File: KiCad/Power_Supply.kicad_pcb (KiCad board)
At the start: 4 copper layers, 59.7 x 64.9 mm, 54 parts, among them IC1 TPS63070RNMR, IC2 ISL23511WFB8Z, IC3 LDO40LPU33RY, J1 Jack-DC, J10 BTM_OUT, J2 USB_B, J3 LCD_connector, J4 SWD, J5 TOP_OUT, U1 STM32F401RBTx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

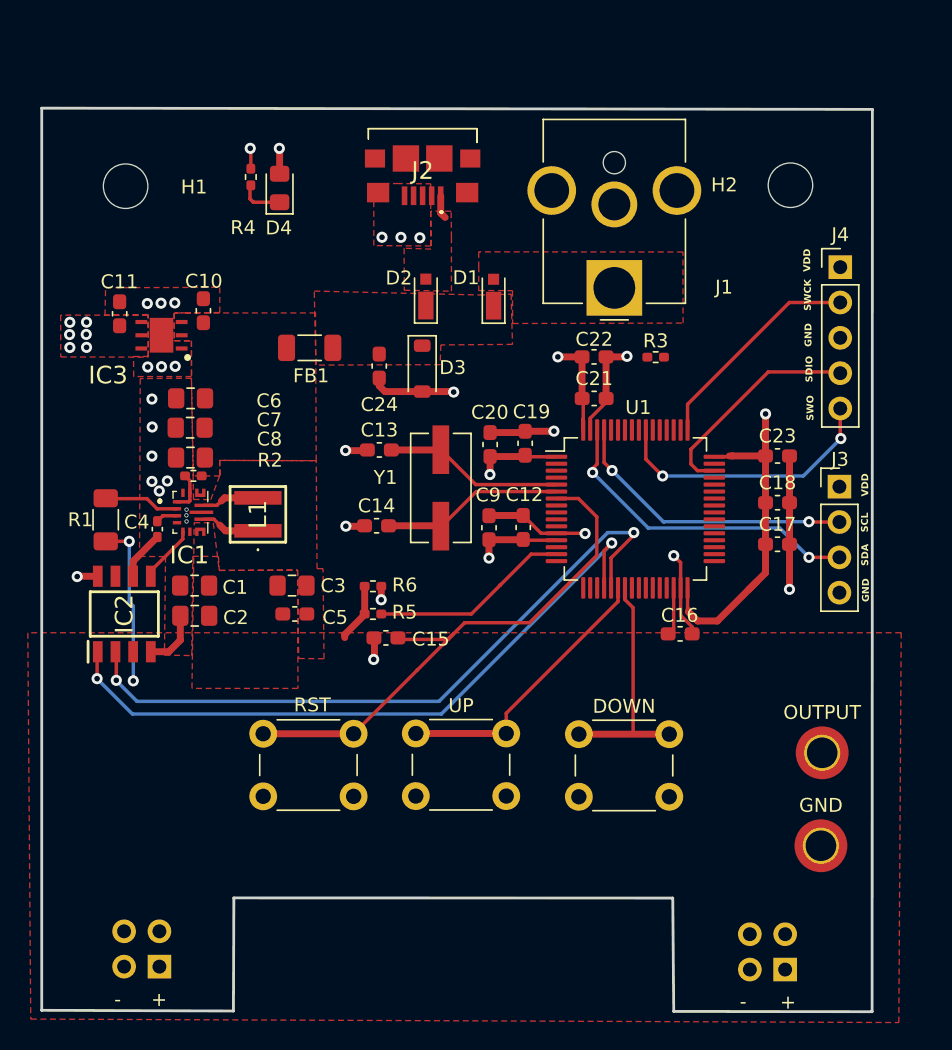
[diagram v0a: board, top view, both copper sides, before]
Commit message: Boot-0 and button layout updated.
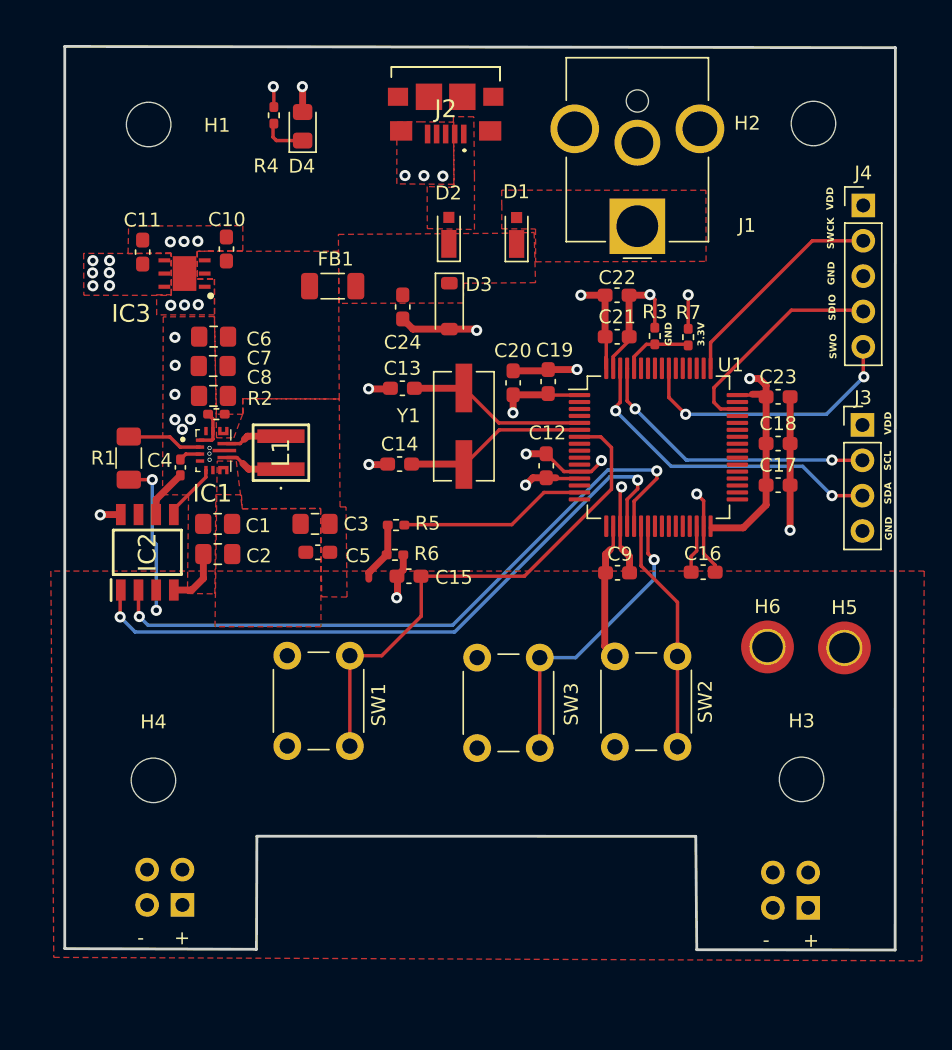
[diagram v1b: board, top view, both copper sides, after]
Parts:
- added H3: MountingHole, MountingHole:MountingHole_3.2mm_M3, F.Cu at (161.8, 100.1)
- added H4: MountingHole, MountingHole:MountingHole_3.2mm_M3, F.Cu at (115.2, 100.2)
- added R7: 1K, Resistor_SMD:R_0402_1005Metric_Pad0.72x0.64mm_HandSolder, F.Cu at (153.7, 68.3)
- D3: value 25V+ -> 30V+
- R5: value 100 -> 300
- R6: value 300 -> 1K2
- moved SW2 19.6 mm to (152.9, 91.3), turned to -90 degrees
- moved H6 14.8 mm to (159.3, 90.6)
- moved C9 9.79 mm to (148.6, 85.3), turned to 0 degrees
- moved H5 7.71 mm to (164.9, 90.7)
- moved R5 6.60 mm to (132.7, 81.8)
- moved SW3 6.18 mm to (143.0, 91.4), turned to -90 degrees
- moved SW1 5.98 mm to (124.8, 97.7), turned to 90 degrees
- moved D3 4.90 mm to (136.5, 66.1)
- moved C1 4.73 mm to (119.8, 81.8)
- moved C13 4.73 mm to (133.1, 72.0)
- moved C14 4.73 mm to (132.9, 77.5)
- moved C16 4.73 mm to (154.7, 85.2)
- moved C19 4.73 mm to (143.6, 71.5)
- moved C20 4.73 mm to (141.1, 71.6)
- moved C21 4.73 mm to (148.5, 68.3)
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- renumbered OUTPUT to H5, GND to H6, RST to SW1, UP to SW2, DOWN to SW3
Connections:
- IC1 pad 16: Main_in -> (no net)
- IC1 pad 17: ADC -> (no net)
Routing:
- net GND: track 56.0 -> 67.8 mm
- net /BOOT: track 0.00 -> 5.14 mm
- net POT_BTN_UP: track 20.3 -> 16.9 mm
- net /NRST: track 39.6 -> 37.6 mm
- net /MCU_POWER/USB_OUT: track 1.70 -> 0.00 mm
- net +3.3V: track 48.7 -> 47.3 mm, vias 12 -> 14
- net PD: track 49.6 -> 48.7 mm
- net Net-(U1-PA1): track 14.4 -> 13.6 mm
- net PU: track 48.6 -> 48.0 mm
- net ADC: track 16.1 -> 15.5 mm
- net POT_BTN_DWN: track 21.2 -> 21.0 mm, vias 0 -> 1
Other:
- board text added: "3.3V"

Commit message: Added some notes and extra ground vias.
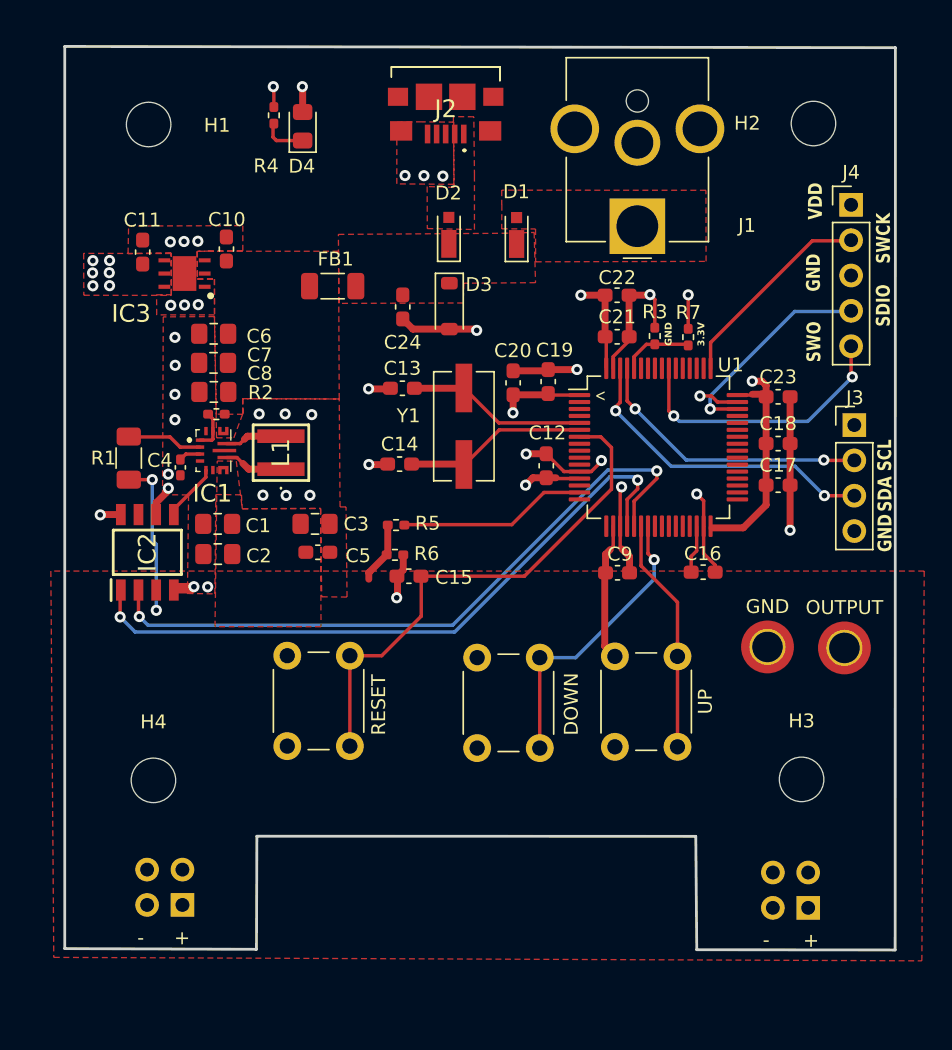
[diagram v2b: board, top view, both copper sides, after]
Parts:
- moved J4 0.88 mm to (165.4, 58.8)
- moved J3 0.59 mm to (165.6, 74.7)
- moved C8 0.29 mm to (119.5, 72.3)
- moved C7 0.23 mm to (119.5, 70.2)
- moved C6 0.21 mm to (119.5, 68.1)
- renumbered SW3 to DOWN, H6 to GND, H5 to OUTPUT, SW1 to RESET, SW2 to UP
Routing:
- net +3.3V: track 47.3 -> 46.2 mm
- net SWCLK: track 15.9 -> 15.0 mm
- net GND: track 67.8 -> 67.3 mm, vias 29 -> 35
- net SWDIO: track 16.0 -> 15.6 mm, vias 0 -> 1
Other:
- board text added: "<"

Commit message: Starting revision 1.1
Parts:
- C24: value 16pF -> 100nF
- C5: footprint Capacitor_SMD:C_0603_1608Metric_Pad1.08x0.95mm_HandSolder -> Capacitor_SMD:C_0805_2012Metric_Pad1.18x1.45mm_HandSolder
- R5: value 300 -> 2K1
- moved R6 2.20 mm to (132.6, 81.8), turned to 0 degrees
- moved R5 2.00 mm to (132.6, 83.8), turned to 0 degrees
- moved C5 0.29 mm to (126.9, 84.1)
- renumbered OUTPUT to H5, GND to H6, RESET to SW1, UP to SW2, DOWN to SW3
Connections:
- R5 pad 1: Net-(U1-PA1) -> ADC
- R5 pad 2: ADC -> Net-(U1-PA1)
- R6 pad 2: ADC -> Net-(U1-PA1)
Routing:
- net GND: track 67.3 -> 69.9 mm
- net Net-(U1-PA1): track 13.6 -> 15.6 mm
- net ADC: track 15.5 -> 14.7 mm
- net SCL: track 21.0 -> 20.4 mm

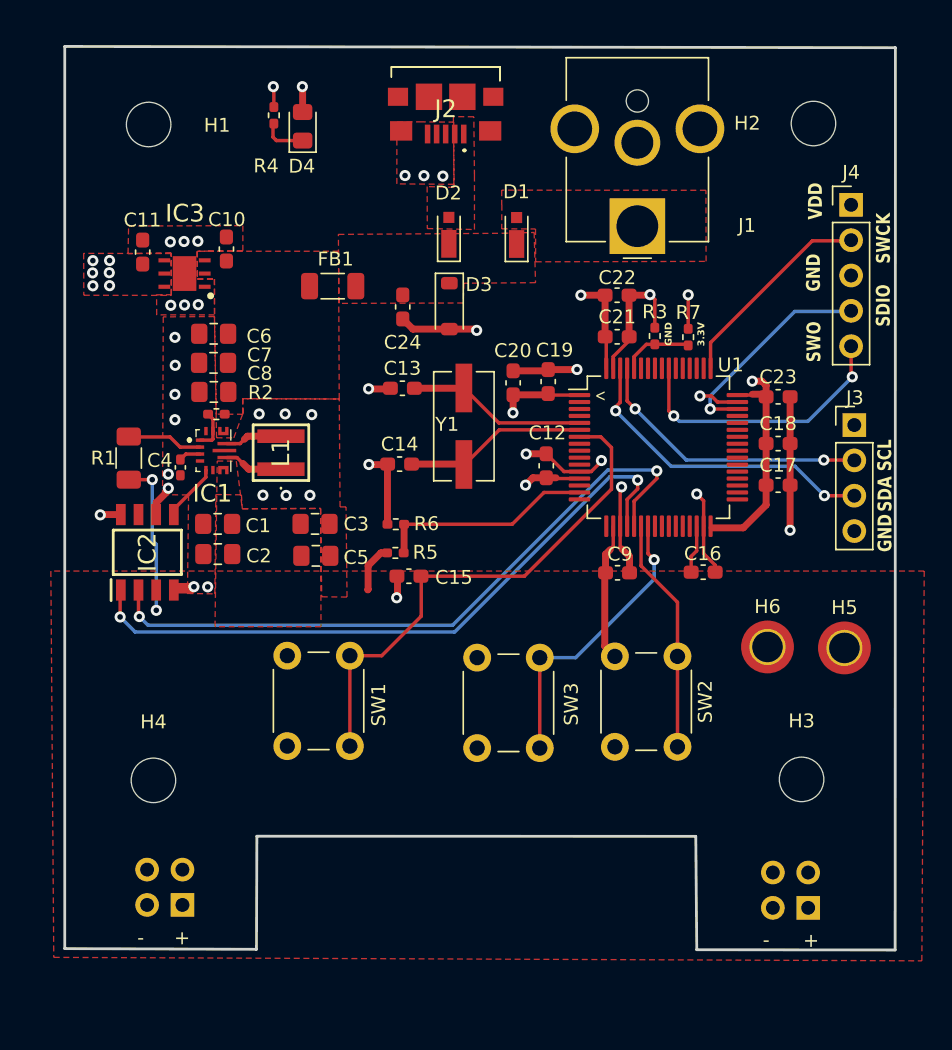
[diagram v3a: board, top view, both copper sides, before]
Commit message: pushing ofr system reset
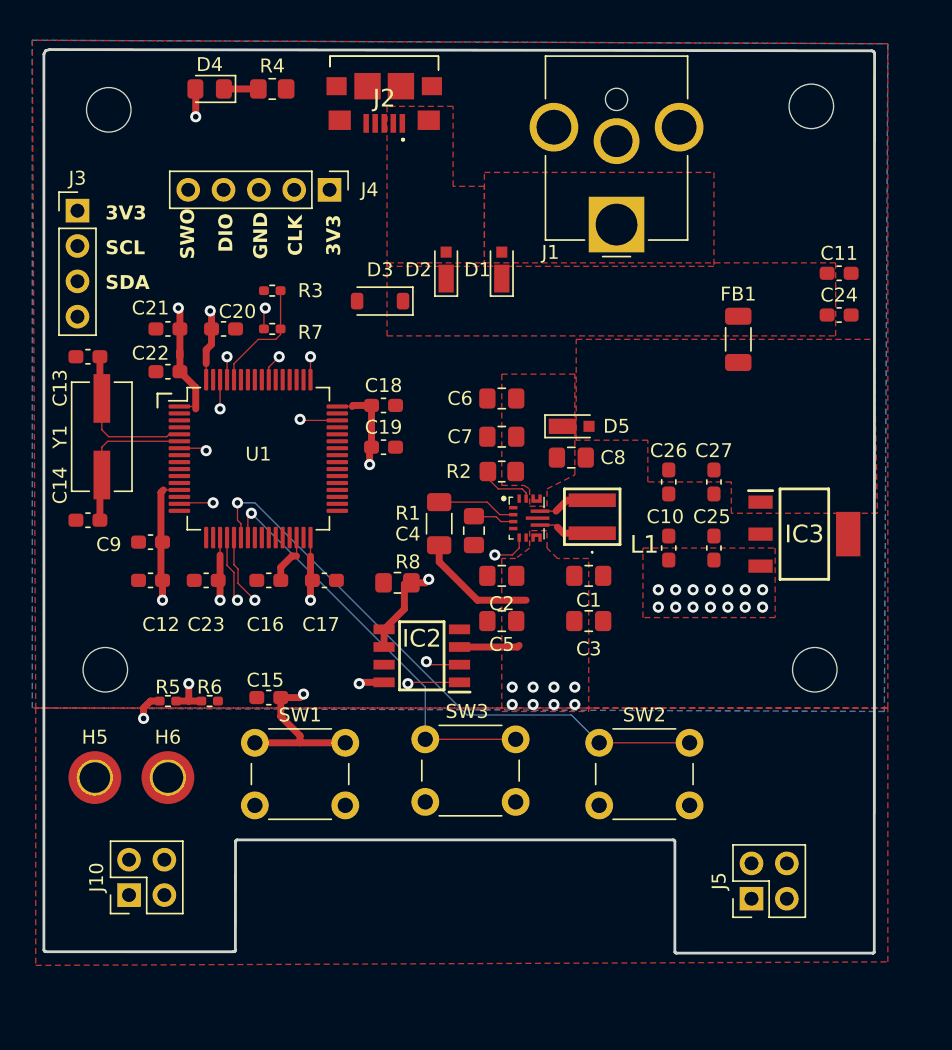
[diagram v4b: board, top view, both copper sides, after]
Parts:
- added C25: .1uF, Capacitor_SMD:C_0603_1608Metric_Pad1.08x0.95mm_HandSolder, F.Cu at (155.5, 83.5)
- added C26: 1uF, Capacitor_SMD:C_0603_1608Metric_Pad1.08x0.95mm_HandSolder, F.Cu at (152.2, 78.8)
- added C27: .1uF, Capacitor_SMD:C_0603_1608Metric_Pad1.08x0.95mm_HandSolder, F.Cu at (155.5, 78.8)
- added D5: D_Schottky, Diode_SMD:D_MicroSMP_AK, F.Cu at (145.5, 74.8)
- added R8: 953, Resistor_SMD:R_0805_2012Metric_Pad1.20x1.40mm_HandSolder, F.Cu at (132.8, 86.0)
- C10, C11: value 4.7uF -> 1uF
- C24: value 100nF -> 1uF
- C4: footprint Capacitor_SMD:C_0402_1005Metric_Pad0.74x0.62mm_HandSolder -> Capacitor_SMD:C_0805_2012Metric_Pad1.18x1.45mm_HandSolder
- IC3: value LDO40LPU33RY -> MCP1754ST-3302E_DB; footprint Custom_eric:SON95P300X300X90-7N-D -> Custom_eric:MCP1754ST-3302E_DB
- J10, J5: moved to F.Cu
- R2, R4: footprint Resistor_SMD:R_0402_1005Metric_Pad0.72x0.64mm_HandSolder -> Resistor_SMD:R_0805_2012Metric_Pad1.20x1.40mm_HandSolder
- moved J3 57.9 mm to (109.8, 59.2)
- moved H5 54.7 mm to (111.0, 100.0)
- moved H3 50.7 mm to (111.8, 92.2)
- moved C11 50.1 mm to (164.5, 63.8), turned to 0 degrees
- moved IC3 48.3 mm to (162.0, 82.5), turned to 0 degrees
- moved H4 48.2 mm to (162.8, 92.2)
- moved H6 44.1 mm to (116.2, 100.0)
- moved C23 43.2 mm to (119.0, 85.8), turned to 180 degrees
- moved C10 38.4 mm to (152.2, 83.5)
- moved J4 37.5 mm to (127.9, 57.8), turned to -90 degrees
- moved C9 33.6 mm to (115.0, 83.1)
- moved C17 33.3 mm to (127.5, 85.8)
- moved C22 32.8 mm to (116.2, 70.8), turned to 180 degrees
- moved C21 32.3 mm to (116.2, 67.8), turned to 180 degrees
- moved C24 31.4 mm to (164.5, 66.8), turned to 0 degrees
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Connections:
- C10 pad 1: Main_in -> +3.3V
- C11 pad 1: +3.3V -> Net-(D1-K)
- C24 pad 1: /MCU_POWER/RAW_FILTER -> Net-(D1-K)
- C6 pad 1: Main_in -> /Output_circuitry/VIN
- C7 pad 1: Main_in -> /Output_circuitry/VIN
- C8 pad 1: Main_in -> /Output_circuitry/VIN
- D1 pad 1: /MCU_POWER/RAW_FILTER -> Net-(D1-K)
- D2 pad 1: /MCU_POWER/RAW_FILTER -> Net-(D1-K)
- D3 pad 1: /MCU_POWER/RAW_FILTER -> Net-(D1-K)
- FB1 pad 1: /MCU_POWER/RAW_FILTER -> Net-(D1-K)
- IC1 pad 1: /Output_circuitry/EN -> GND
- IC1 pad 12: Main_in -> /Output_circuitry/VIN
- IC1 pad 13: Main_in -> /Output_circuitry/VIN
- IC2 pad 6: GND -> Wiper
- IC3 pad 1: GND -> Main_in
- IC3 pad 2: Main_in -> GND
- IC3 pad 3: Main_in -> +3.3V
- IC3 pad 4: +3.3V -> GND
- R2 pad 2: Main_in -> /Output_circuitry/VIN
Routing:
- net GND: track 69.9 -> 0.00 mm, vias 35 -> 0
- net PD: track 48.7 -> 22.3 mm
- net POT_BTN_UP: track 16.9 -> 42.2 mm, vias 0 -> 1
- net PU: track 48.0 -> 23.3 mm
- net Wiper: track 4.16 -> 15.2 mm, vias 0 -> 2
- net POT_BTN_DWN: track 21.0 -> 29.8 mm
- net SDA: track 23.5 -> 16.9 mm, vias 2 -> 1
- net SWDIO: track 15.6 -> 21.5 mm
- net SCL: track 20.4 -> 15.7 mm, vias 2 -> 1
- net Net-(U1-PA1): track 15.6 -> 19.2 mm, vias 0 -> 2
- net SWO: track 20.1 -> 16.7 mm, vias 2 -> 1
- net /BOOT: track 5.14 -> 8.52 mm
- net /NRST: track 37.6 -> 34.6 mm, vias 0 -> 2
- net Net-(U1-PH1): track 13.1 -> 11.1 mm
- net Net-(U1-PH0): track 12.9 -> 11.2 mm
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- added copper zone on B.Cu, net +3.3V
- added copper zone on F.Cu, net /Output_circuitry/VIN
- added copper zone on In1.Cu, net ADC
- added copper zone on F.Cu, net Net-(D1-K)
- removed copper zone on In2.Cu, net +3.3V
- removed copper zone on F.Cu, net /MCU_POWER/RAW_FILTER
- removed copper zone on In1.Cu, net GND
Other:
- board size 59.7 x 64.9 mm -> 59.7 x 65 mm
- board text added: "3V3"
- board text added: "CLK"
- board text added: "DIO"
- board text removed: "+"
- board text removed: "-"
- board text removed: "3.3V"
- board text removed: "<"
- board text removed: "SDIO"
- board text removed: "SWCK"
- board text removed: "VDD"

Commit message: Replaced pot.
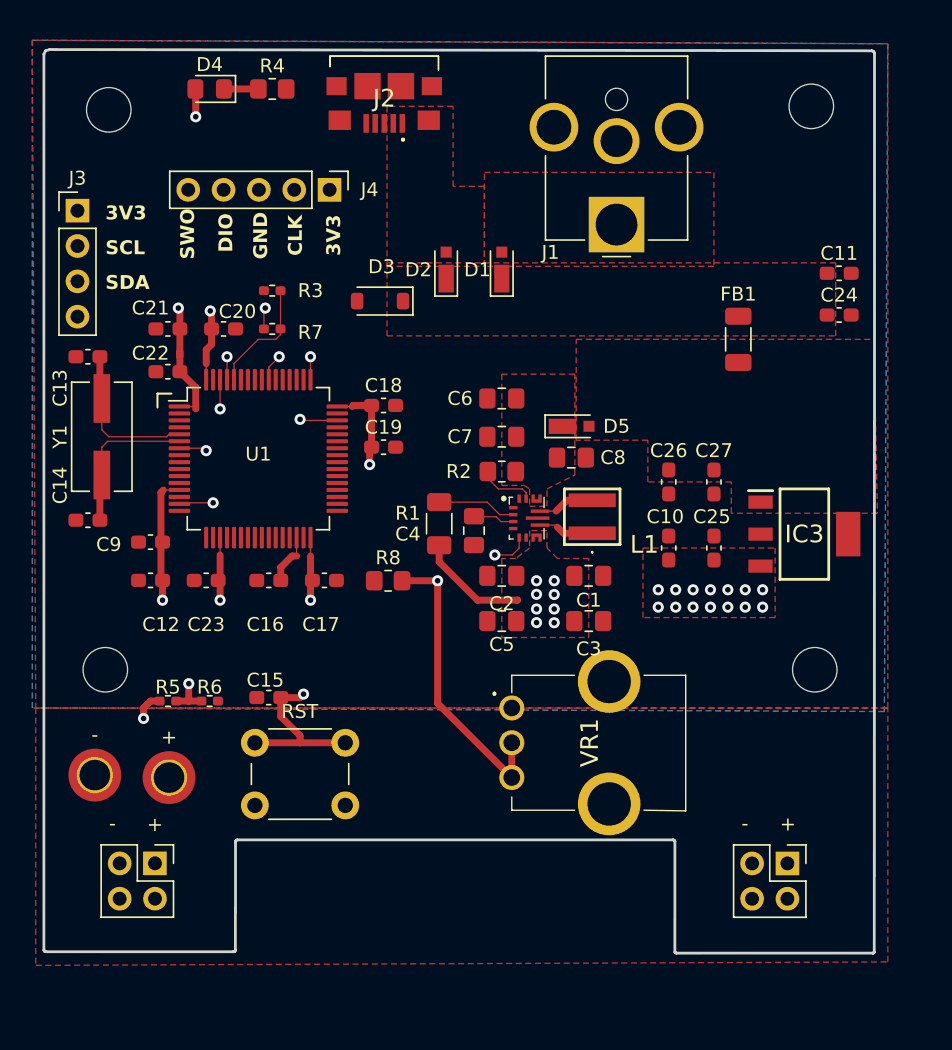
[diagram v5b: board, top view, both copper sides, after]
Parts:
- removed IC2: ISL23511WFB8Z, Custom_eric:ISL23511WFB8Z
- removed SW2: POT_UP, Button_Switch_THT:SW_PUSH_6mm_H4.3mm
- removed SW3: POT_DWN, Button_Switch_THT:SW_PUSH_6mm_H4.3mm
- added VR1: PTV09A-1015U-B203, SamacSys_Parts:PTV09A1015UB203, F.Cu at (141.0, 95.0)
- R5: value 2K1 -> 1K
- R6: value 1K2 -> 500
- R8: value 953 -> 2K
- moved + 5.33 mm to (116.3, 100.0)
- moved - 5.26 mm to (111.0, 99.8)
- moved J5 3.62 mm to (160.8, 106.2), turned to -90 degrees
- moved + 2.94 mm to (115.3, 106.2), turned to -90 degrees
- moved R8 0.69 mm to (132.1, 85.9), turned to 0 degrees
- renumbered J10 to +, H5 to +, H6 to -, SW1 to RST
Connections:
- IC1 pad 5: Wiper -> CW
- R8 pad 1: Wiper -> GND
- R8 pad 2: GND -> CW
- U1 pad 20: PU -> unconnected-(U1-PA4-Pad20)
- U1 pad 21: PD -> unconnected-(U1-PA5-Pad21)
- U1 pad 22: POT_BTN_UP -> unconnected-(U1-PA6-Pad22)
- U1 pad 23: POT_BTN_DWN -> unconnected-(U1-PA7-Pad23)
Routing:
- net POT_BTN_UP: track 42.2 -> 0.00 mm, vias 1 -> 0
- net CW: track 0.00 -> 29.9 mm, vias 0 -> 2
- net POT_BTN_DWN: track 29.8 -> 0.00 mm, vias 1 -> 0
- net PU: track 23.3 -> 0.00 mm, vias 2 -> 0
- net PD: track 22.3 -> 0.00 mm, vias 2 -> 0
- net Wiper: track 15.2 -> 0.00 mm, vias 2 -> 0
- net ADC: track 15.0 -> 10.1 mm
- net +3.3V: track 44.8 -> 43.0 mm, vias 23 -> 22
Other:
- board text added: "+"
- board text added: "-"
